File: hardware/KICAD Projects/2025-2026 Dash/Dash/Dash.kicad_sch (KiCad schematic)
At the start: 33 parts, among them IC1 MCP25625-E_SS, J1 TACH-SERVO, J2 SPEED-SERVO, J3 5V INPUT, J4 UPPER Button, J5 TO CAN CONNECTOR, J6 LOWER Button, U1 XIAO-ESP32-S3-SMD, U3 EA DOGM128W-6, Y1 ABM10AIG-16.000MHZ-4Z-T3

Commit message: Dash R1 Milestone
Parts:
- removed J3: 5V INPUT, Connector_Wire:SolderWire-0.75sqmm_1x02_P4.8mm_D1.25mm_OD2.3mm, symbol Connector:Conn_01x02_Pin
- removed J5: TO CAN CONNECTOR, Connector_Wire:SolderWire-0.75sqmm_1x04_P4.8mm_D1.25mm_OD2.3mm, symbol Connector_Generic:Conn_01x04
- added J7: DTF13-6P, DTF13-6P:TE_DTF13-6P, symbol DTF13-6P:DTF13-6P
- LOWER_AlphaDriver2, UPPER_AlphaDriver2: footprint Adafruit HT16K33 Breakout:DIP1778W100P254L3556H630Q28N -> Adafruit HT16K33 Breakout (Laptop):DIP1778W100P254L3556H630Q28N
- LOWER_D1-2, LOWER_D3-4, UPPER_D1-2, UPPER_D3-4: footprint Adafruit Dual Alphanumeric LED:1908 -> Adafruit Dual Alphanumeric LED (Laptop):1908
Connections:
- net +5V: now also J7.1
- net CAN_HIGH: now also J7.4, J7.6
- net CAN_LOW: now also J7.3, J7.5
- net GND: now also J7.2; no longer IC1.26 (VSS)
- new net CAN_GND: IC1.26 (VSS)

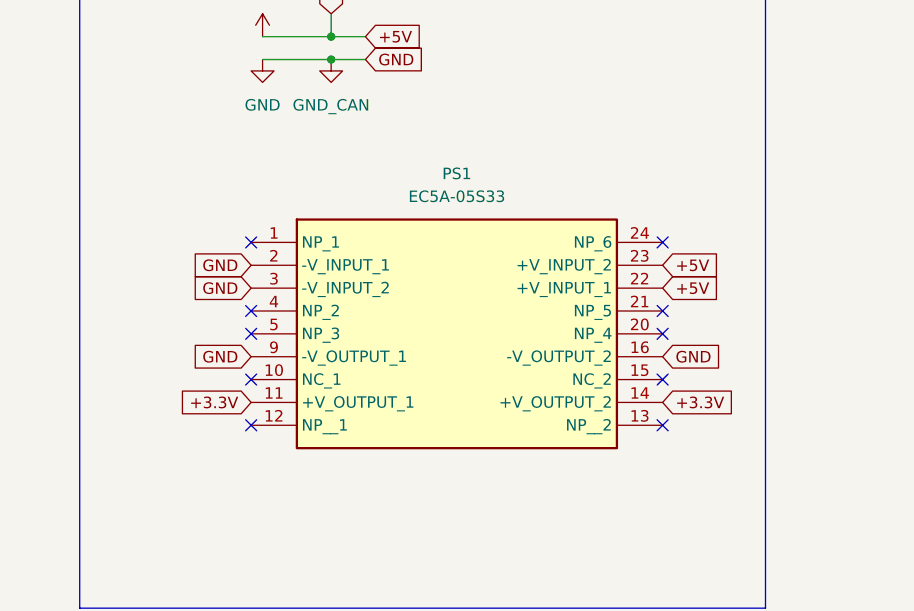
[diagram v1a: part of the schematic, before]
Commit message: Voltage Converter Modification
Old 5V-3.3V NON-isolated converter was out of stock everywhere, replaced it with ISOLATED unit with GNDs connected together lol
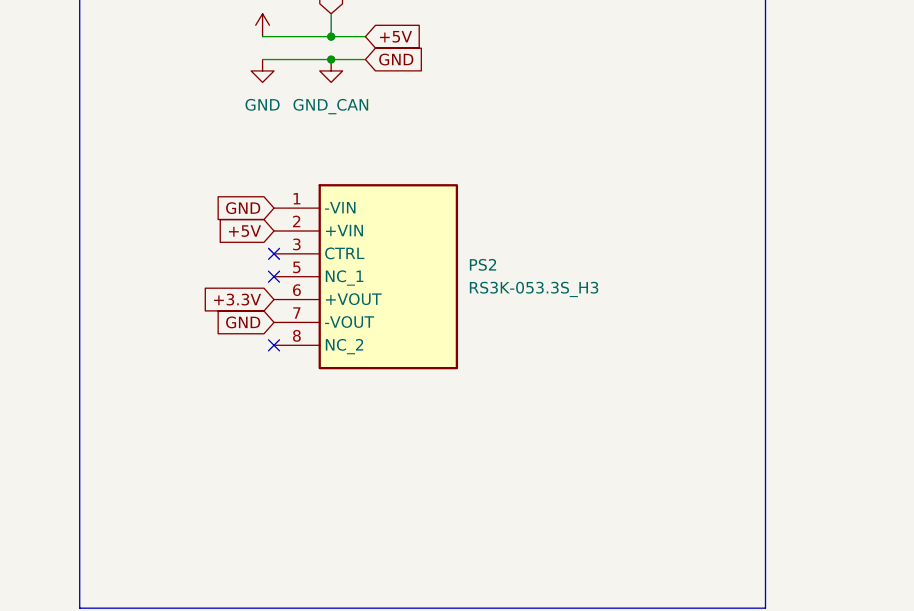
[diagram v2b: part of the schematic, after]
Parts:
- removed PS1: EC5A-05S33, EC5A-05S33:EC5A05S33, symbol EC5A-05S33:EC5A-05S33
- added PS2: RS3K-053.3S_H3, RS3K-053.3S_H3:RS3K0533SH3, symbol RS3K-053_3S_H3:RS3K-053.3S_H3
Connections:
- net +3.3V: now also PS2.6 (+VOUT)
- net +5V: now also PS2.2 (+VIN)
- net GND: now also PS2.1 (-VIN), PS2.7 (-VOUT)
- no-connect marks 44 -> 37
